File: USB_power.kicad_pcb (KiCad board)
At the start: 2 copper layers, 42.5 x 65.5 mm, 30 parts, among them J1 PWR_IN, J2 USB_A_Stacked, J3 Power_check, J4 USB_C_Receptacle_USB2.0_16P, J5 USB_A

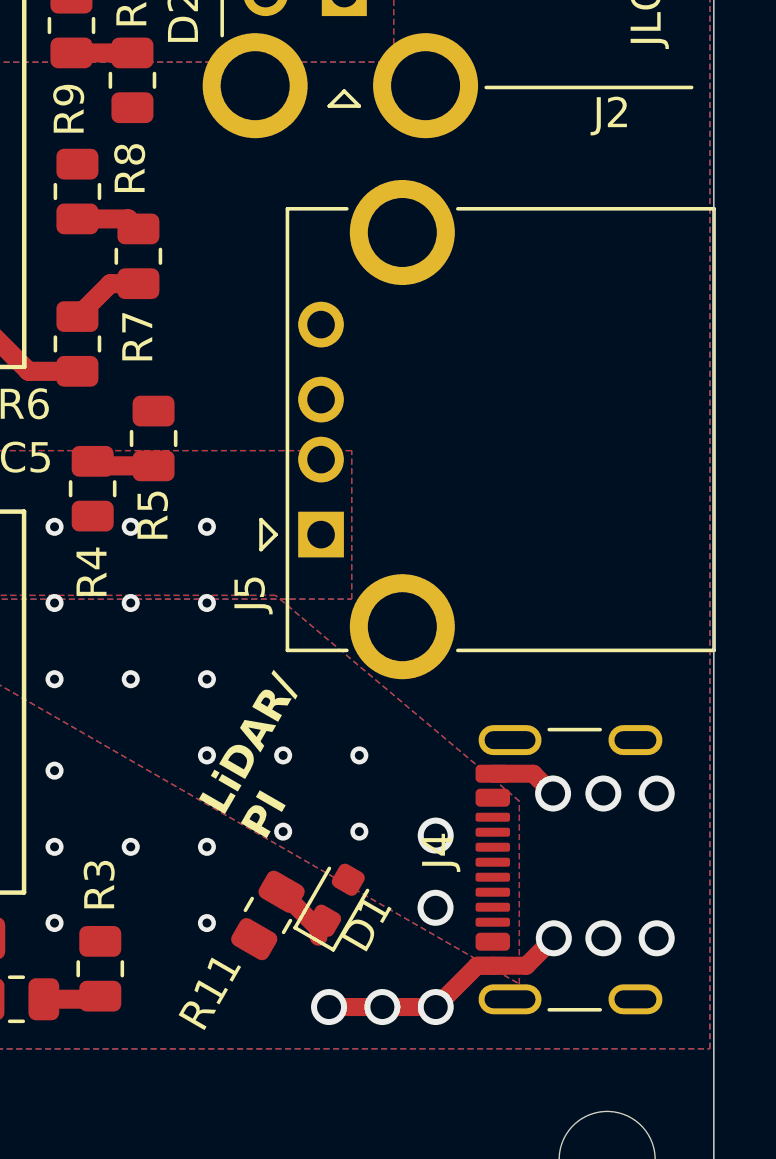
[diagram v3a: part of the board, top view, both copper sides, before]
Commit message: PCB: MD1系統スタックコネクタに変更
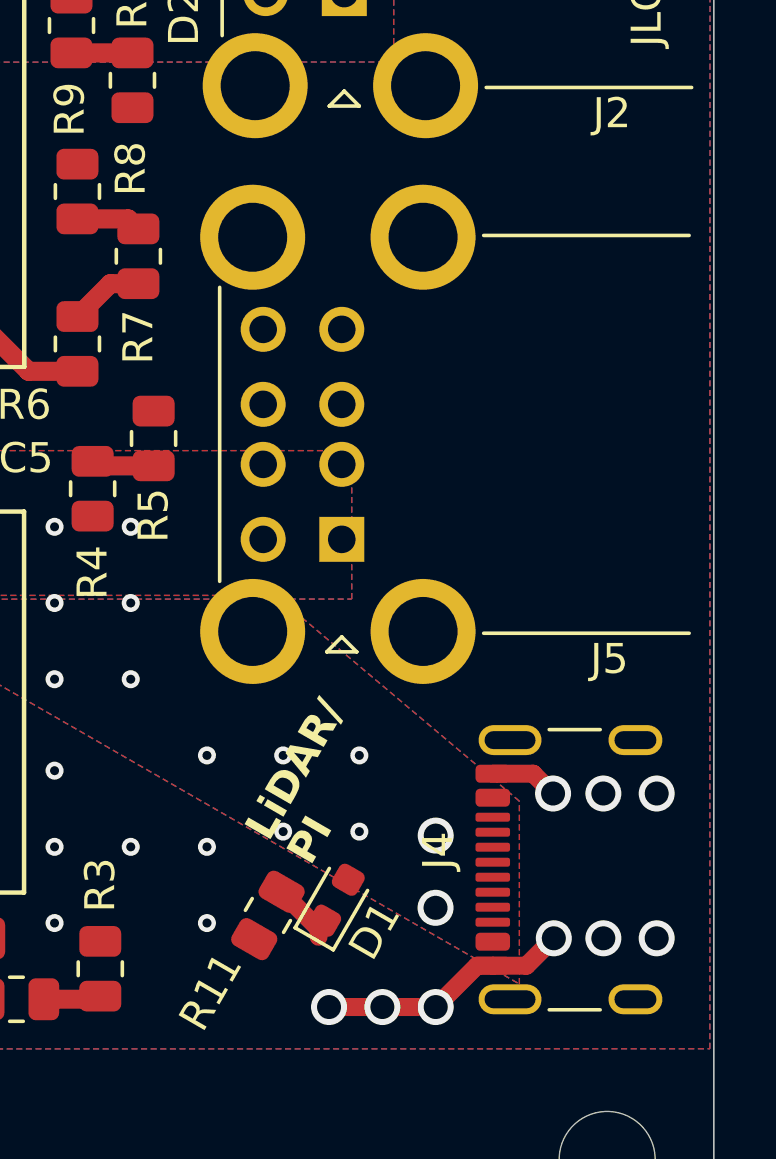
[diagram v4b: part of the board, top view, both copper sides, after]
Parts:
- J5: value USB_A -> USB_A_Stacked; footprint Connector_USB:USB_A_CONNFLY_DS1095-WNR0 -> Connector_USB:USB_A_CUI_UJ2-ADH-TH_Horizontal_Stacked
- moved J5 0.71 mm to (157.9, 113.2), turned to 180 degrees
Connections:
- J5 pad 5: unconnected-(J5-Shield-Pad5) -> +5V
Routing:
- net +5V: vias 16 -> 13

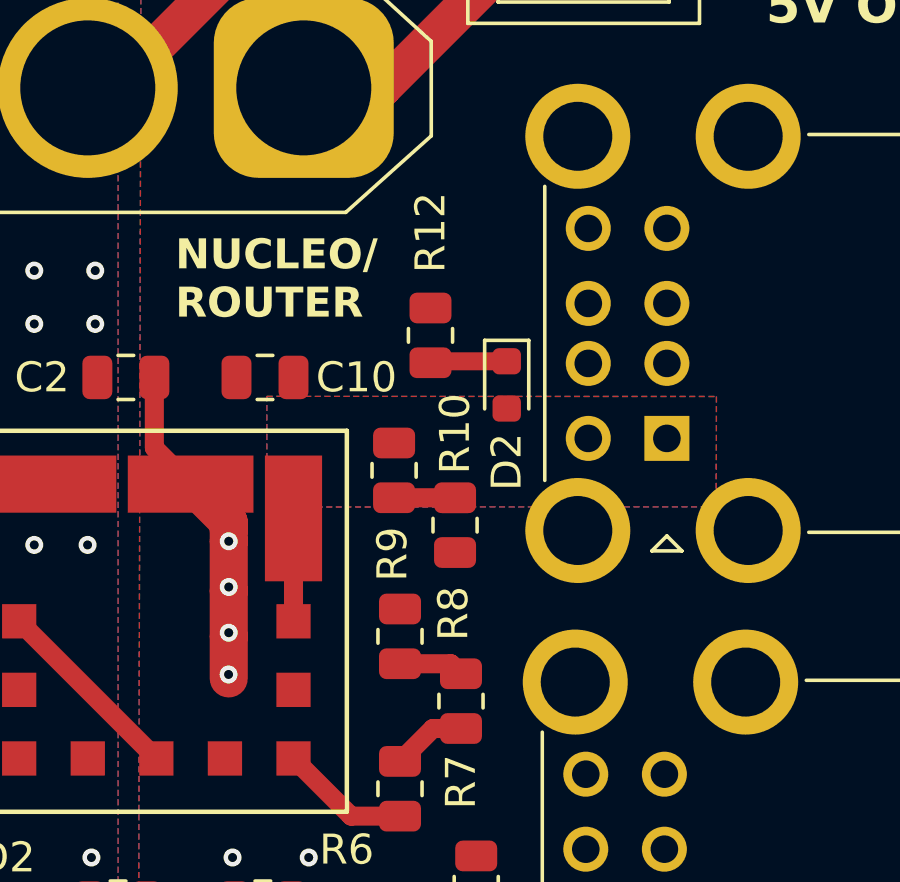
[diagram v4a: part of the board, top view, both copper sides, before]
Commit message: 部品配置調整、XT60にMask追加
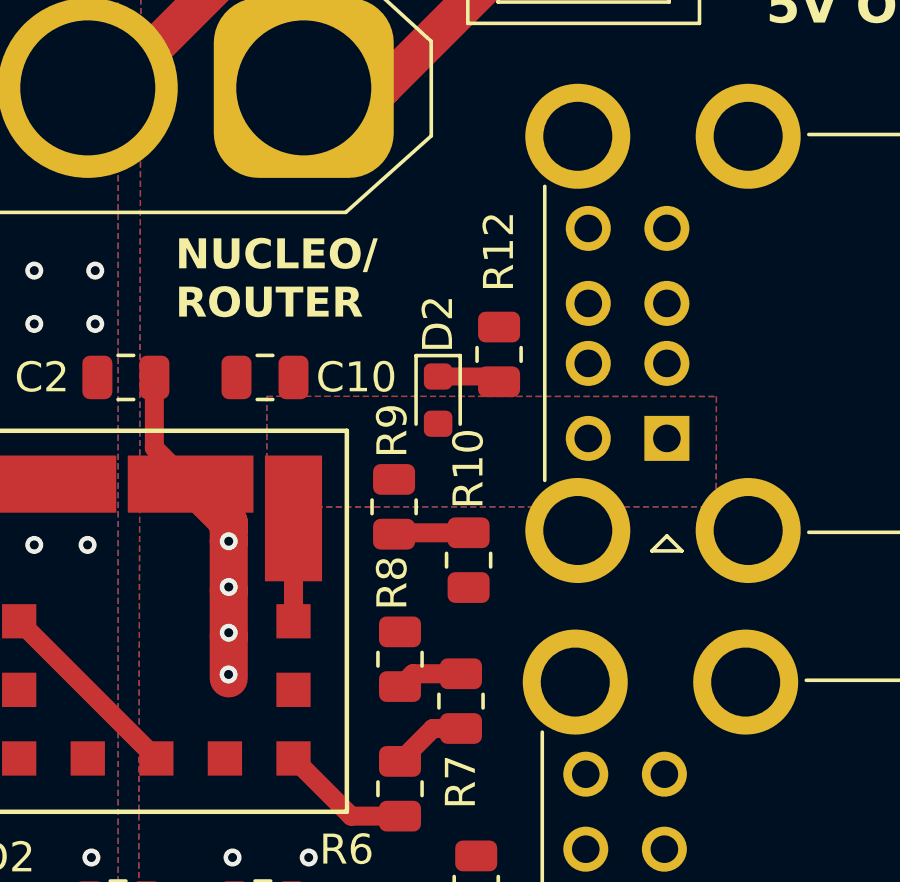
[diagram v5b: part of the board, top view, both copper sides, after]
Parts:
- moved R12 2.37 mm to (152.4, 92.2)
- moved D2 2.34 mm to (150.4, 93.7)
- moved R10 1.25 mm to (151.4, 99.1)
- moved R9 1.22 mm to (148.9, 97.3)
- moved R8 0.76 mm to (149.1, 102.4)
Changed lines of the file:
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@@
 	(footprint "Resistor_SMD:R_0805_2012Metric"
 		(layer "F.Cu")
-		(at 148.900318 96.0666 -90)
+		(at 148.900318 97.282 -90)
 		(descr "Resistor SMD 0805 (2012 Metric), square (rectangular) end terminal, IPC_7351 nominal, (Body size source: IPC-SM-782 page 72, https://www.pcb-3d.com/wordpress/wp-content/uploads/ipc-sm-782a_amendment_1_and_2.pdf), generated with kicad-footprint-generator")
 		(tags "resistor")
 		(property "Reference" "R9"
-			(at 2.7921 0.056318 90)
+			(at -2.54 0.056318 90)
 			(layer "F.SilkS")
 			(effects
@@
 	(footprint "Resistor_SMD:R_0805_2012Metric"
 		(layer "F.Cu")
-		(at 150.932318 97.8935 -90)
+		(at 151.384 99.06 -90)
 		(descr "Resistor SMD 0805 (2012 Metric), square (rectangular) end terminal, IPC_7351 nominal, (Body size source: IPC-SM-782 page 72, https://www.pcb-3d.com/wordpress/wp-content/uploads/ipc-sm-782a_amendment_1_and_2.pdf), generated with kicad-footprint-generator")
 		(tags "resistor")
@@
 	(footprint "LED_SMD:LED_0603_1608Metric"
 		(layer "F.Cu")
-		(at 152.654 93.218 -90)
+		(at 150.368 93.726 -90)
 		(descr "LED SMD 0603 (1608 Metric), square (rectangular) end terminal, IPC_7351 nominal, (Body size source: http://www.tortai-tech.com/upload/download/2011102023233369053.pdf), generated with kicad-footprint-generator")
 		(tags "LED")
 		(property "Reference" "D2"
-			(at 2.5655 0 90)
+			(at -2.54 0 90)
 			(layer "F.SilkS")
 			(effects
@@
 	(footprint "Resistor_SMD:R_0805_2012Metric"
 		(layer "F.Cu")
-		(at 149.098 101.6 90)
+		(at 149.098 102.362 90)
 		(descr "Resistor SMD 0805 (2012 Metric), square (rectangular) end terminal, IPC_7351 nominal, (Body size source: IPC-SM-782 page 72, https://www.pcb-3d.com/wordpress/wp-content/uploads/ipc-sm-782a_amendment_1_and_2.pdf), generated with kicad-footprint-generator")
 		(tags "resistor")
 		(property "Reference" "R8"
-			(at 0.762 1.778 90)
+			(at 2.54 -0.254 90)
 			(layer "F.SilkS")
 			(effects
@@
 	(footprint "Resistor_SMD:R_0805_2012Metric"
 		(layer "F.Cu")
-		(at 150.114 91.567 90)
+		(at 152.4 92.202 90)
 		(descr "Resistor SMD 0805 (2012 Metric), square (rectangular) end terminal, IPC_7351 nominal, (Body size source: IPC-SM-782 page 72, https://www.pcb-3d.com/wordpress/wp-content/uploads/ipc-sm-782a_amendment_1_and_2.pdf), generated with kicad-footprint-generator")
 		(tags "resistor")
@@
 		)
 	)
+	(gr_circle
+		(center 138.43 83.312)
+		(end 141.224 85.344)
+		(stroke
+			(width 0.1)
+			(type default)
+		)
+		(fill solid)
+		(layer "B.Mask")
+	)
+	(gr_rect
+		(start 142.494 79.756)
+		(end 149.479 86.868)
+		(stroke
+			(width 0.1)
+			(type default)
+		)
+		(fill solid)
+		(layer "B.Mask")
+	)
 	(gr_line
 		(start 131.217518 71.887518)
@@
 	)
 	(segment
-		(start 150.796 102.5125)
+		(start 149.526 102.8465)
 		(end 151.13 102.8465)
 		(width 0.635)
@@
 	)
 	(segment
-		(start 149.098 102.5125)
-		(end 150.796 102.5125)
+		(start 149.098 103.2745)
+		(end 149.526 102.8465)
 		(width 0.635)
 		(layer "F.Cu")
@@
 	)
 	(segment
-		(start 148.900318 96.9791)
-		(end 150.930418 96.9791)
+		(start 148.900318 98.1945)
+		(end 148.947318 98.1475)
 		(width 0.635)
 		(layer "F.Cu")
@@
 	)
 	(segment
-		(start 150.930418 96.9791)
-		(end 150.932318 96.981)
+		(start 148.947318 98.1475)
+		(end 151.384 98.1475)
 		(width 0.635)
 		(layer "F.Cu")
@@
 	)
 	(segment
-		(start 150.163 92.4305)
-		(end 152.654 92.4305)
+		(start 152.224 92.9385)
+		(end 150.368 92.9385)
 		(width 0.6)
 		(layer "F.Cu")
@@
 	)
 	(segment
-		(start 150.114 92.4795)
-		(end 150.163 92.4305)
+		(start 152.4 93.1145)
+		(end 152.224 92.9385)
 		(width 0.6)
 		(layer "F.Cu")

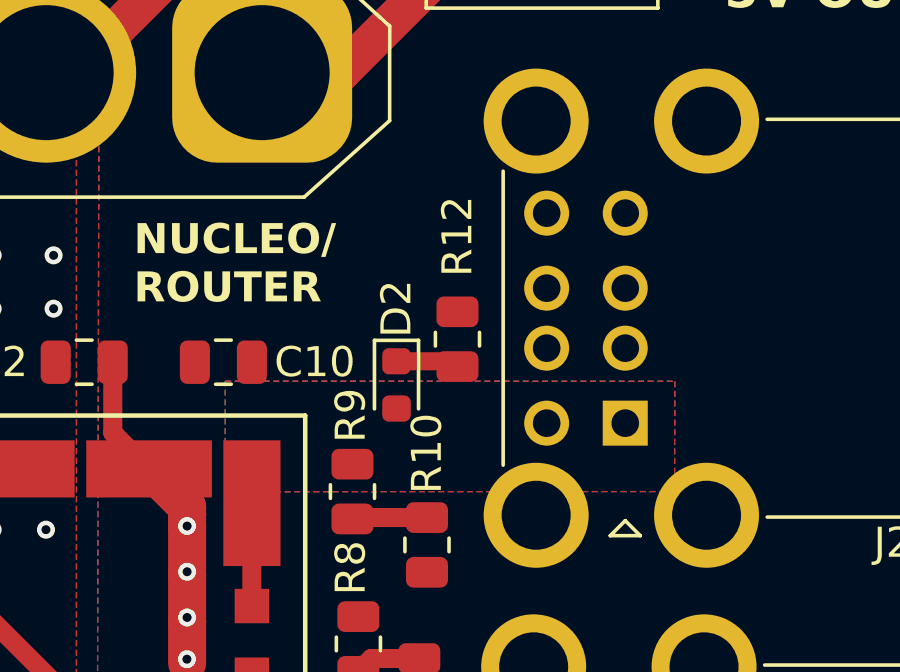
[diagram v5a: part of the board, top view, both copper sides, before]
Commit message: MD2系統 5V出力手前ビア追加
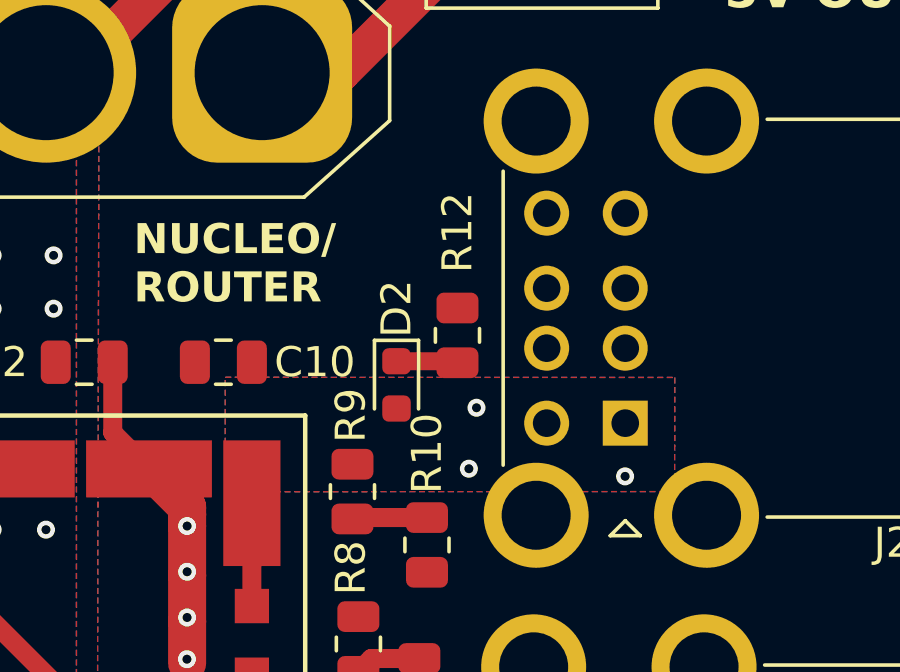
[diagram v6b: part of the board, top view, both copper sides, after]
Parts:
- moved R12 0.13 mm to (152.4, 92.1)
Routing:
- net +5VP: vias 0 -> 3
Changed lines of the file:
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@@
 		(tags "resistor")
 		(property "Reference" "R2"
-			(at -2.6905 0 360)
+			(at -2.6905 0 0)
 			(layer "F.SilkS")
 			(effects
@@
 		)
 		(property "Value" "330R"
-			(at -2.9445 0 360)
+			(at -2.9445 0 0)
 			(layer "F.Fab")
 			(effects
@@
 		)
 		(fp_text user "${REFERENCE}"
-			(at 0 0 360)
+			(at 0 0 0)
 			(layer "F.Fab")
 			(effects
@@
 		(tags "resistor")
 		(property "Reference" "R1"
-			(at -2.6435 -0.127 360)
+			(at -2.6435 -0.127 0)
 			(layer "F.SilkS")
 			(effects
@@
 		)
 		(property "Value" "1k"
-			(at 2.54 0 360)
+			(at 2.54 0 0)
 			(layer "F.Fab")
 			(effects
@@
 		)
 		(fp_text user "${REFERENCE}"
-			(at 0 0 360)
+			(at 0 0 0)
 			(layer "F.Fab")
 			(effects
@@
 	(footprint "Resistor_SMD:R_0805_2012Metric"
 		(layer "F.Cu")
-		(at 152.4 92.202 90)
+		(at 152.4 92.075 90)
 		(descr "Resistor SMD 0805 (2012 Metric), square (rectangular) end terminal, IPC_7351 nominal, (Body size source: IPC-SM-782 page 72, https://www.pcb-3d.com/wordpress/wp-content/uploads/ipc-sm-782a_amendment_1_and_2.pdf), generated with kicad-footprint-generator")
 		(tags "resistor")
@@
 		(tags "USB-A CUI stacked horizontal through-hole")
 		(property "Reference" "J5"
-			(at -8.92 -3.99 360)
+			(at -8.92 -3.99 0)
 			(layer "F.SilkS")
 			(effects
@@
 		)
 		(property "Value" "USB_A_Stacked"
-			(at -2.2 14.18 360)
+			(at -2.2 14.18 0)
 			(layer "F.Fab")
 			(effects
@@
 		)
 		(fp_text user "${REFERENCE}"
-			(at -4.535 3.5 360)
+			(at -4.535 3.5 0)
 			(layer "F.Fab")
 			(effects
@@
 	)
 	(segment
-		(start 152.224 92.9385)
-		(end 150.368 92.9385)
+		(start 152.4 92.9875)
+		(end 152.351 92.9385)
 		(width 0.6)
 		(layer "F.Cu")
@@
 	)
 	(segment
-		(start 152.4 93.1145)
-		(end 152.224 92.9385)
+		(start 152.351 92.9385)
+		(end 150.368 92.9385)
 		(width 0.6)
 		(layer "F.Cu")
@@
 		(net 44)
 	)
+	(via
+		(at 153.035 94.488)
+		(size 0.6)
+		(drill 0.3)
+		(layers "F.Cu" "B.Cu")
+		(free yes)
+		(net 44)
+	)
+	(via
+		(at 157.988 96.774)
+		(size 0.6)
+		(drill 0.3)
+		(layers "F.Cu" "B.Cu")
+		(free yes)
+		(net 44)
+	)
+	(via
+		(at 152.781 96.52)
+		(size 0.6)
+		(drill 0.3)
+		(layers "F.Cu" "B.Cu")
+		(free yes)
+		(net 44)
+	)
 	(zone
 		(net 1)
@@
 		(polygon
 			(pts
-				(xy 144.658518 97.287518) (xy 144.658518 93.599) (xy 159.644518 93.604518) (xy 159.639 97.282)
+				(xy 144.658518 97.287518) (xy 144.658518 93.472) (xy 159.644518 93.477518) (xy 159.639 97.282)
 			)
 		)

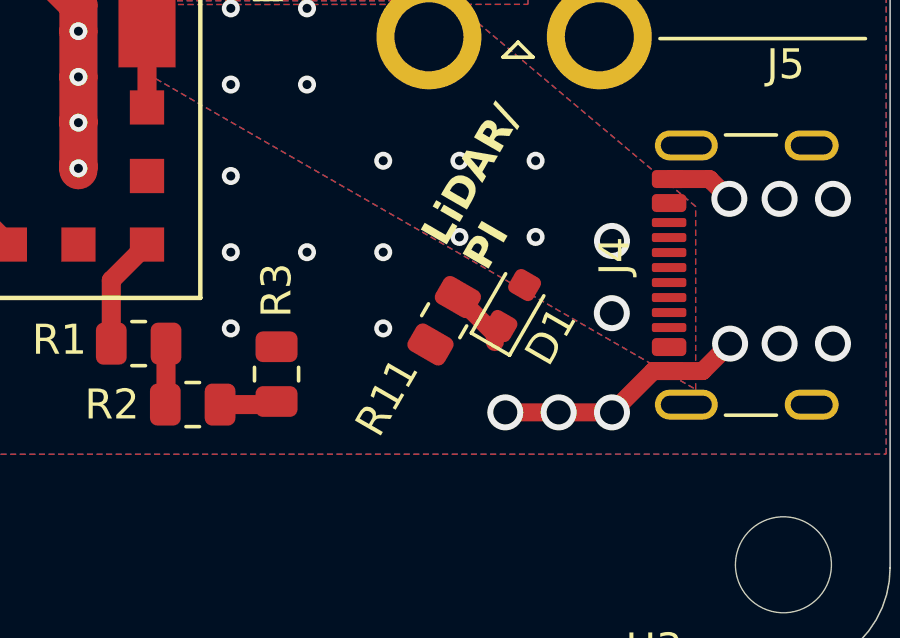
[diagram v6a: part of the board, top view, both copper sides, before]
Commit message: USB-C周りGNDベタ幅改善
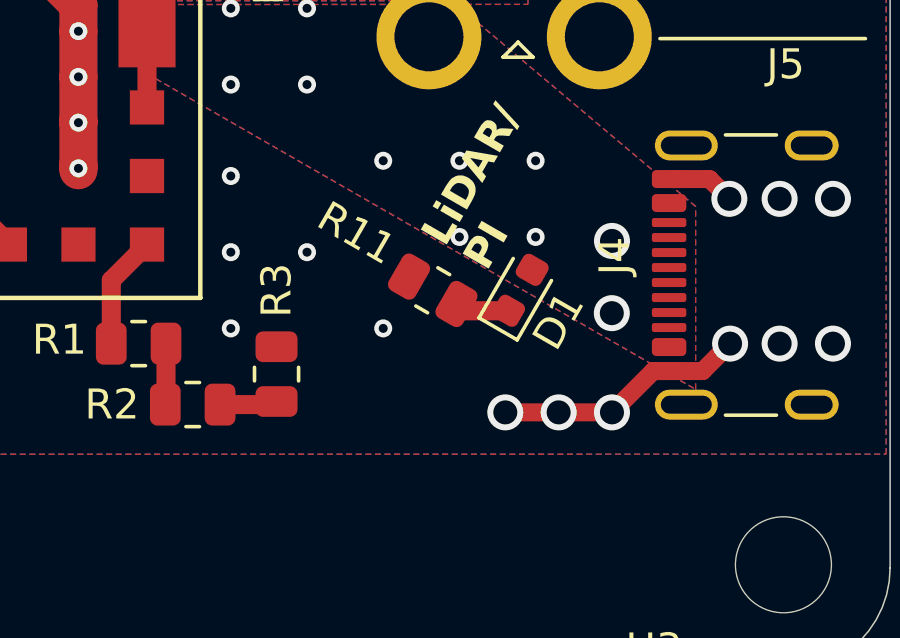
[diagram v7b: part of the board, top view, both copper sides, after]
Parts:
- moved R11 1.09 mm to (155.1, 124.7), turned to 150 degrees
- moved D1 0.57 mm to (158.0, 124.7)
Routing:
- net GND: vias 25 -> 24
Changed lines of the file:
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@@
 	(footprint "LED_SMD:LED_0603_1608Metric"
 		(layer "F.Cu")
-		(at 157.734 125.222 60)
+		(at 157.988 124.714 60)
 		(descr "LED SMD 0603 (1608 Metric), square (rectangular) end terminal, IPC_7351 nominal, (Body size source: http://www.tortai-tech.com/upload/download/2011102023233369053.pdf), generated with kicad-footprint-generator")
 		(tags "LED")
@@
 	(footprint "Resistor_SMD:R_0805_2012Metric"
 		(layer "F.Cu")
-		(at 155.448 125.73 -120)
+		(at 155.067 124.714 150)
 		(descr "Resistor SMD 0805 (2012 Metric), square (rectangular) end terminal, IPC_7351 nominal, (Body size source: IPC-SM-782 page 72, https://www.pcb-3d.com/wordpress/wp-content/uploads/ipc-sm-782a_amendment_1_and_2.pdf), generated with kicad-footprint-generator")
 		(tags "resistor")
 		(property "Reference" "R11"
-			(at 3.152205 0.379778 60)
+			(at 3.152205 0.379778 150)
 			(layer "F.SilkS")
 			(effects
@@
 		)
 		(property "Value" "10k"
-			(at -0.9525 -1.649778 60)
+			(at -0.9525 -1.649778 150)
 			(layer "F.Fab")
 			(effects
@@
 		)
 		(property "Footprint" "Resistor_SMD:R_0805_2012Metric"
-			(at 0 0 -120)
+			(at 0 0 150)
 			(unlocked yes)
 			(layer "F.Fab")
@@
 		)
 		(property "Datasheet" ""
-			(at 0 0 -120)
+			(at 0 0 150)
 			(unlocked yes)
 			(layer "F.Fab")
@@
 		)
 		(property "Description" "Resistor"
-			(at 0 0 -120)
+			(at 0 0 150)
 			(unlocked yes)
 			(layer "F.Fab")
@@
 		(attr smd)
 		(fp_line
-			(start -0.227064 0.735)
-			(end 0.227064 0.735)
+			(start -0.227064 -0.735)
+			(end 0.227064 -0.735)
 			(stroke
 				(width 0.12)
@@
 		)
 		(fp_line
-			(start -0.227064 -0.735)
-			(end 0.227064 -0.735)
+			(start -0.227064 0.735)
+			(end 0.227064 0.735)
 			(stroke
 				(width 0.12)
@@
 		)
 		(fp_line
-			(start 1.68 0.95)
-			(end -1.68 0.95)
+			(start 1.68 -0.95)
+			(end 1.68 0.95)
 			(stroke
 				(width 0.05)
@@
 		)
 		(fp_line
-			(start 1.68 -0.95)
-			(end 1.68 0.95)
+			(start 1.68 0.95)
+			(end -1.68 0.95)
 			(stroke
 				(width 0.05)
@@
 		)
 		(fp_line
-			(start -1.68 0.95)
-			(end -1.68 -0.95)
+			(start -1.68 -0.95)
+			(end 1.68 -0.95)
 			(stroke
 				(width 0.05)
@@
 		)
 		(fp_line
-			(start -1.68 -0.95)
-			(end 1.68 -0.95)
+			(start -1.68 0.95)
+			(end -1.68 -0.95)
 			(stroke
 				(width 0.05)
@@
 		)
 		(fp_line
-			(start 1 0.625)
-			(end -1 0.625)
+			(start 1 -0.625)
+			(end 1 0.625)
 			(stroke
 				(width 0.1)
@@
 		)
 		(fp_line
-			(start -1 0.625)
-			(end -1 -0.625)
+			(start 1 0.625)
+			(end -1 0.625)
 			(stroke
 				(width 0.1)
@@
 		)
 		(fp_line
-			(start 1 -0.625)
-			(end 1 0.625)
+			(start -1 -0.625)
+			(end 1 -0.625)
 			(stroke
 				(width 0.1)
@@
 		)
 		(fp_line
-			(start -1 -0.625)
-			(end 1 -0.625)
+			(start -1 0.625)
+			(end -1 -0.625)
 			(stroke
 				(width 0.1)
@@
 		)
 		(fp_text user "${REFERENCE}"
-			(at 0 0 60)
+			(at 0 0 150)
 			(layer "F.Fab")
 			(effects
@@
 		)
 		(pad "1" smd roundrect
-			(at -0.9125 0 240)
+			(at -0.9125 0 150)
 			(size 1.025 1.4)
 			(layers "F.Cu" "F.Paste" "F.Mask")
@@
 		)
 		(pad "2" smd roundrect
-			(at 0.9125 0 240)
+			(at 0.9125 0 150)
 			(size 1.025 1.4)
 			(layers "F.Cu" "F.Paste" "F.Mask")
@@
 	)
 	(via
-		(at 153.416 123.444)
-		(size 0.6)
-		(drill 0.3)
-		(layers "F.Cu" "B.Cu")
-		(free yes)
-		(net 1)
-	)
-	(via
 		(at 148.336 125.984)
 		(size 0.6)
@@
 	)
 	(segment
-		(start 157.138 126.173502)
-		(end 157.138 126.440244)
-		(width 0.6)
+		(start 156.082994 125.395996)
+		(end 155.857248 125.17025)
+		(width 0.635)
 		(layer "F.Cu")
 		(net 33)
 	)
 	(segment
-		(start 155.90425 124.939752)
-		(end 157.138 126.173502)
-		(width 0.6)
+		(start 157.594249 125.395996)
+		(end 156.082994 125.395996)
+		(width 0.635)
 		(layer "F.Cu")
 		(net 33)
